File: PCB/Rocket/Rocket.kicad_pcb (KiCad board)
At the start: 2 copper layers, 62.7 x 63.5 mm, 47 parts, among them J1 Conn_01x08_Pin, J2 Conn_01x04_Pin, J3 Conn_01x07_Pin, J4 Micro_SD_Card, J5 Conn_ARM_JTAG_SWD_10, J6 Conn_01x04_Pin, J7 1987724, SW1 CK_KMS2xxG, SW2 CK_KMS2xxG, U1 STM32L476RGTx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

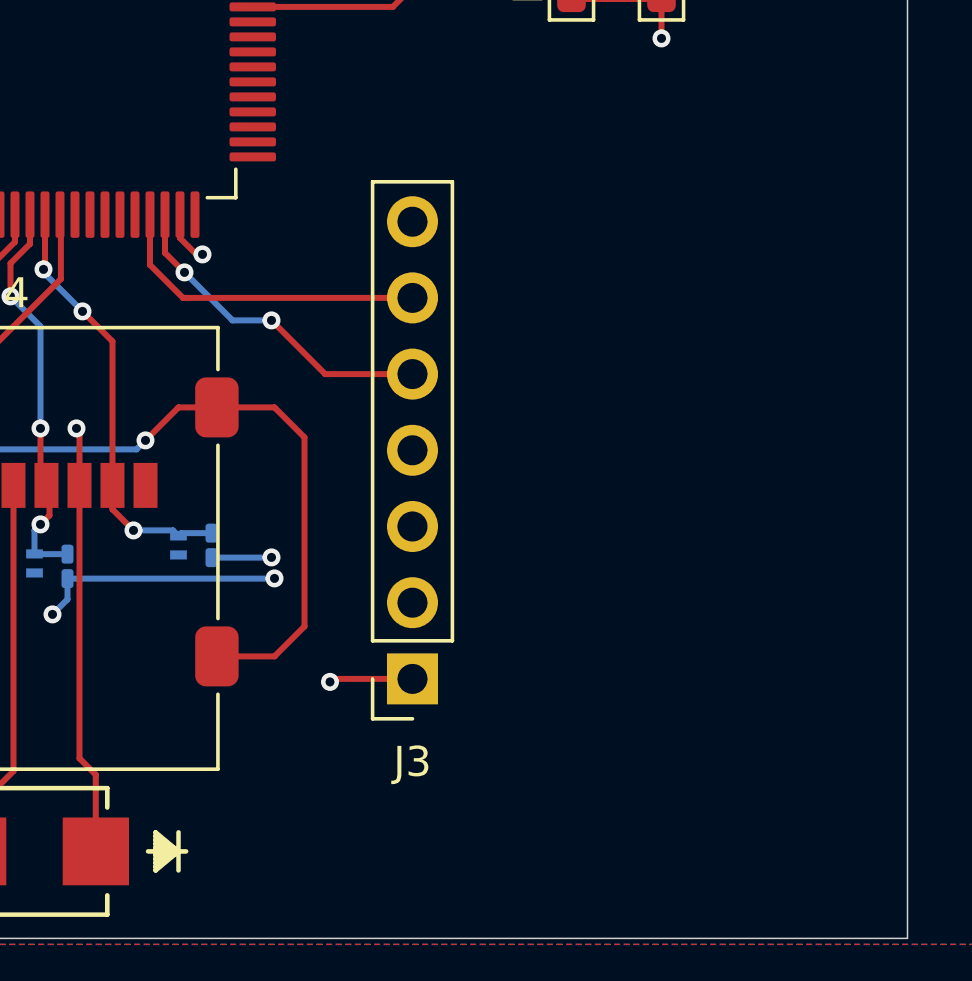
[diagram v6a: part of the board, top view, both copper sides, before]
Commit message: Fixed UART traces.
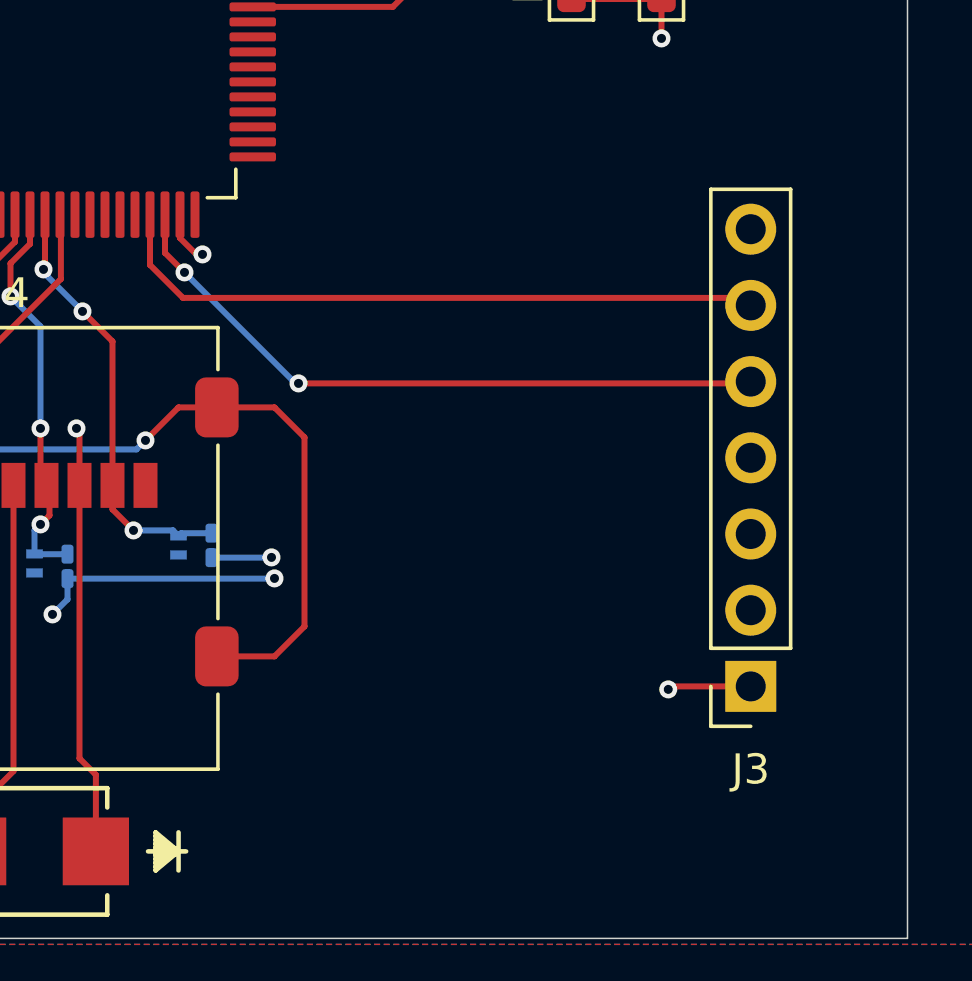
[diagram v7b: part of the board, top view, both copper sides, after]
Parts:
- moved J3 11.3 mm to (160.3, 91.9)
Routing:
- net /RX: track 11.2 -> 22.6 mm
- net /TX: track 11.5 -> 22.9 mm
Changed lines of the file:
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@@
 	(footprint "Connector_PinSocket_2.54mm:PinSocket_1x07_P2.54mm_Vertical"
 		(layer "F.Cu")
-		(at 149 91.65 180)
+		(at 160.275 91.9 180)
 		(descr "Through hole straight socket strip, 1x07, 2.54mm pitch, single row (from Kicad 4.0.7), script generated")
 		(tags "Through hole socket strip THT 1x07 2.54mm single row")
@@
 	)
 	(segment
-		(start 144.3 79.7)
-		(end 146.09 81.49)
+		(start 160.215 81.8)
+		(end 145.2 81.8)
 		(width 0.2)
 		(layer "F.Cu")
@@
 	)
 	(segment
-		(start 146.09 81.49)
-		(end 149 81.49)
+		(start 160.275 81.74)
+		(end 160.215 81.8)
 		(width 0.2)
 		(layer "F.Cu")
@@
 	)
 	(via
-		(at 144.3 79.7)
+		(at 145.2 81.8)
 		(size 0.6)
 		(drill 0.3)
@@
 	)
 	(segment
-		(start 143 79.7)
-		(end 144.3 79.7)
+		(start 145.1 81.8)
+		(end 145.2 81.8)
 		(width 0.2)
 		(layer "B.Cu")
@@
 	(segment
 		(start 141.4 78.1)
-		(end 143 79.7)
+		(end 145.1 81.8)
 		(width 0.2)
 		(layer "B.Cu")
@@
 	)
 	(segment
-		(start 148.55 78.5)
-		(end 149 78.95)
+		(start 141.35 78.95)
+		(end 160.025 78.95)
 		(width 0.2)
 		(layer "F.Cu")
@@
 	)
 	(segment
-		(start 140.25 77.85)
-		(end 141.35 78.95)
+		(start 159.825 78.75)
+		(end 160.275 79.2)
 		(width 0.2)
 		(layer "F.Cu")
@@
 	)
 	(segment
-		(start 141.35 78.95)
-		(end 149 78.95)
+		(start 140.25 76.175)
+		(end 140.25 77.85)
 		(width 0.2)
 		(layer "F.Cu")
@@
 	)
 	(segment
-		(start 140.25 76.175)
-		(end 140.25 77.85)
+		(start 140.25 77.85)
+		(end 141.35 78.95)
+		(width 0.2)
+		(layer "F.Cu")
+		(net 17)
+	)
+	(segment
+		(start 160.025 78.95)
+		(end 160.275 79.2)
 		(width 0.2)
 		(layer "F.Cu")
@@
 	)
 	(segment
-		(start 145.4 89.9)
-		(end 145.4 83.6)
+		(start 128.73 82.6)
+		(end 131.2 82.6)
 		(width 0.2)
 		(layer "F.Cu")
@@
 	)
 	(segment
-		(start 128.73 82.6)
-		(end 131.2 82.6)
+		(start 145.4 89.9)
+		(end 145.4 83.6)
 		(width 0.2)
 		(layer "F.Cu")
@@
 	)
 	(segment
-		(start 146.25 91.75)
-		(end 146.2 91.8)
+		(start 157.525 92)
+		(end 157.475 92.05)
 		(width 0.2)
 		(layer "F.Cu")
@@
 	)
 	(segment
-		(start 146.35 91.65)
-		(end 146.25 91.75)
+		(start 157.625 91.9)
+		(end 157.525 92)
 		(width 0.2)
 		(layer "F.Cu")
@@
 	)
 	(segment
-		(start 149 91.65)
-		(end 146.35 91.65)
+		(start 160.275 91.9)
+		(end 157.625 91.9)
 		(width 0.2)
 		(layer "F.Cu")
@@
 	)
 	(via
-		(at 146.25 91.75)
+		(at 157.525 92)
 		(size 0.6)
 		(drill 0.3)
